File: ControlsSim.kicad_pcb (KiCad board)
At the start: 2 copper layers, 100 x 100 mm, 26 parts, among them J2 Accelerator Pot, J3 Brake Button, J5 Motor Contactors, J6 Array Contactors, J7 Rotary Switch, SW2 SW_Rotary2x6

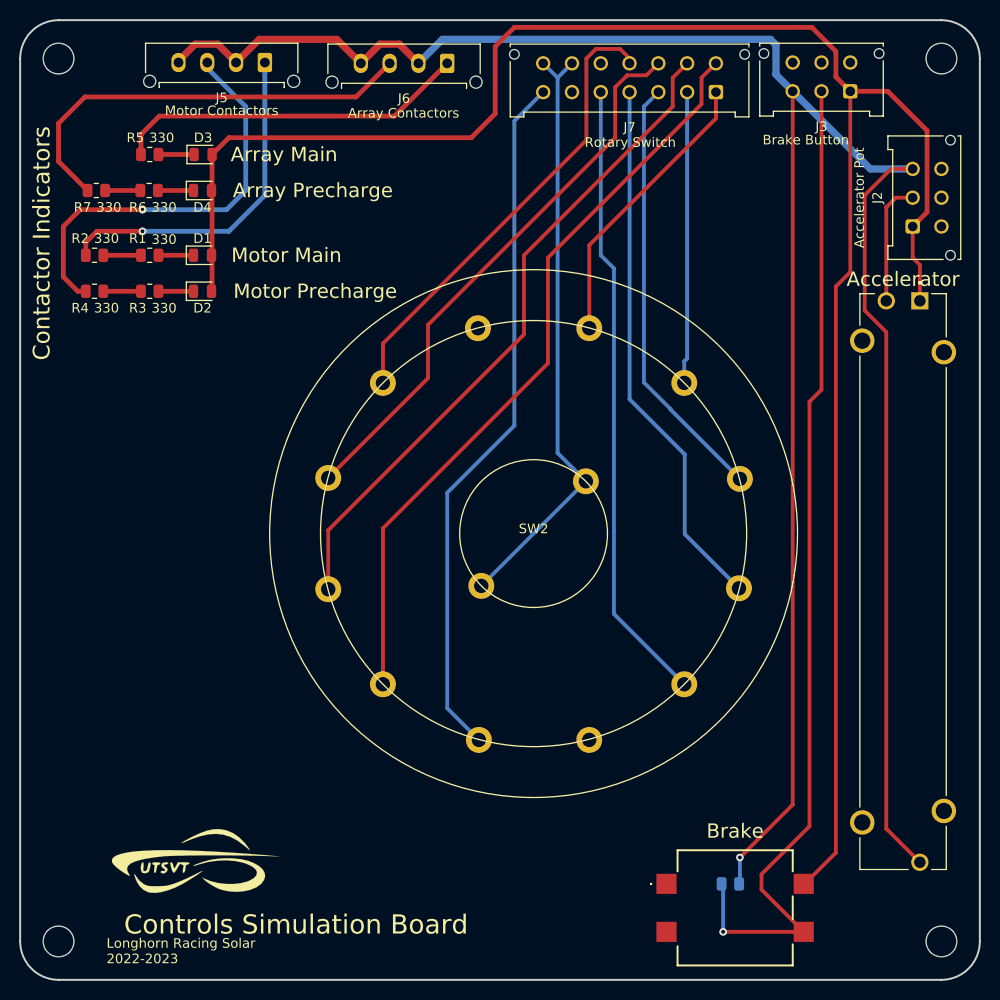
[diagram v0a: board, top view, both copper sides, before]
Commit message: Fixed directories for footprints and 3D models, also fixed incorrect footprint and 3d model for rotary encoder.
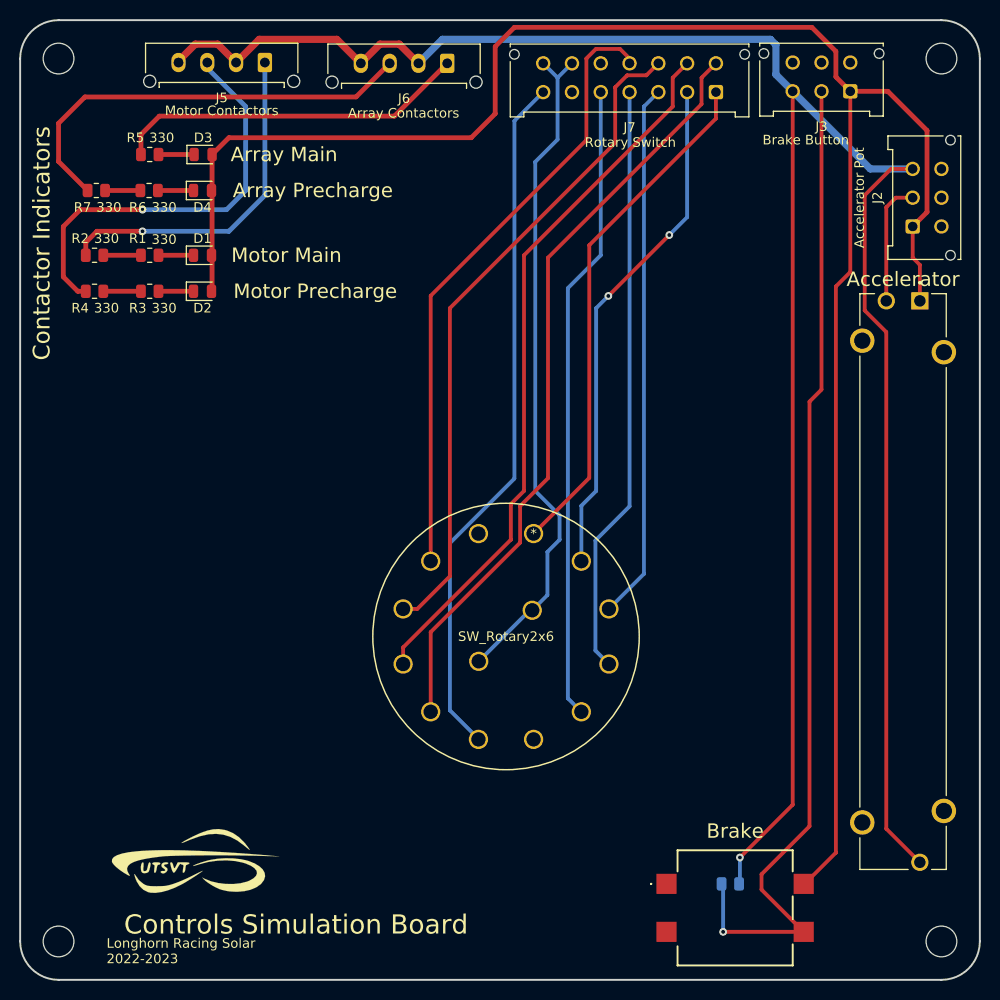
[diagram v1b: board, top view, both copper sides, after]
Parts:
- SW2: footprint Footprints:CK1035 -> UTSVT_Special:CK1035_resized
- moved LOGO1 13.9 mm to (151.1, 111.8)
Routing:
- net /Rot1: track 30.1 -> 53.9 mm
- net /Rot2: track 30.4 -> 53.4 mm, vias 0 -> 2
- net /Rot11: track 48.4 -> 64.9 mm
- net /Rot10: track 58.6 -> 69.9 mm
- net /Rot3: track 45.1 -> 56.0 mm
- net /RotV+: track 62.9 -> 71.1 mm
- net /Rot4: track 56.4 -> 61.6 mm
- net /Rot9: track 70.3 -> 74.9 mm
- net /Rot5: track 65.3 -> 66.6 mm
- net /Rot8: track 79.1 -> 79.9 mm
